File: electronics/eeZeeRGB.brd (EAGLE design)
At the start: 15.7 x 6.6 mm, 5 parts

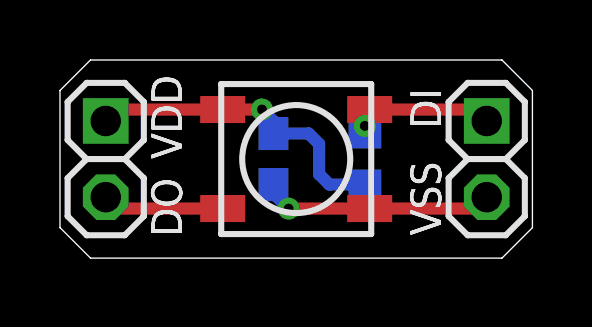
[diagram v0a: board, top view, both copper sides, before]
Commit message: added solder jumper to disable 10k pullup, moved passives layout, minor silk changes, changed silk for ws2812b
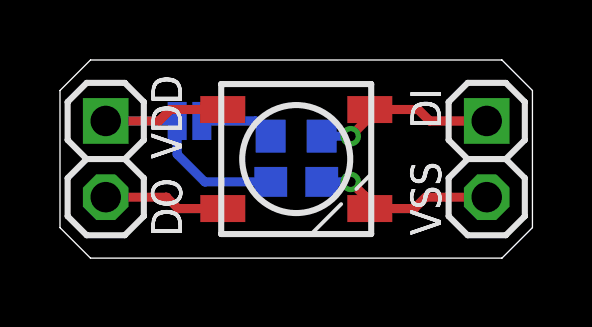
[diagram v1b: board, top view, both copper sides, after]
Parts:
- added SJ1: P/U?, SparkFun-Retired:SJ_2S
- moved R1 2.41 mm to (7.87, 4.06), turned to 0 degrees
- moved C1 1.08 mm to (7.87, 2.54), turned to 180 degrees
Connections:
- new net N$1: R1.2, SJ1.2
- net VDD: now also SJ1.1; no longer R1.2
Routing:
- net N$1: track 0.00 -> 2.50 mm
- net GND: track 7.77 -> 6.17 mm
- net DIN: track 4.88 -> 6.17 mm
- net VDD: track 10.7 -> 11.1 mm, vias 1 -> 0
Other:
- board text added: "R0.2"

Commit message: silk fixes for passives, shrunk board width, fixed version silk, moved pin labels after mirroring pin headers
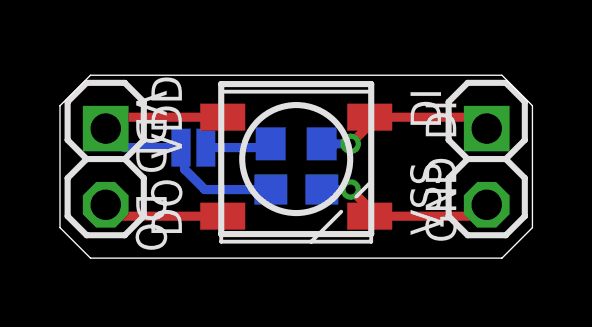
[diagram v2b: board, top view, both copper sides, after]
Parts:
- moved SJ1 0.90 mm to (4.45, 3.68)
- moved C1 0.25 mm to (7.87, 2.29)
- moved JP1 0.25 mm to (1.52, 3.05), flipped to the bottom
- moved JP2 0.25 mm to (14.2, 3.05), flipped to the bottom
- moved LED1 0.25 mm to (7.87, 3.05)
- moved R1 0.25 mm to (7.87, 3.81)
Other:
- board size 15.7 x 6.6 mm -> 15.7 x 6.1 mm
- board text added: "GND"
- board text added: "goo.gl/1GzN6m"

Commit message: Increased width to accommodate minimum width rule from OSHpark
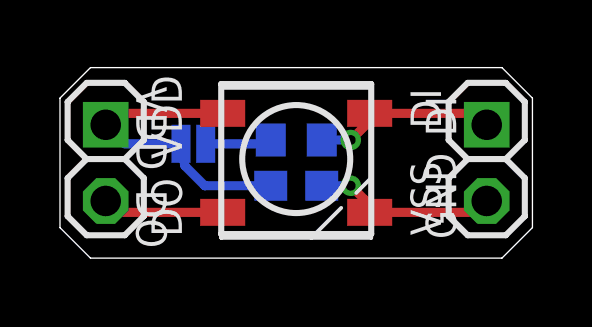
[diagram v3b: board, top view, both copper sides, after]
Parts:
- moved SJ1 0.13 mm to (4.45, 3.81)
- moved C1 0.13 mm to (7.87, 2.41)
- moved JP1 0.13 mm to (1.52, 3.17)
- moved JP2 0.13 mm to (14.2, 3.17)
- moved LED1 0.13 mm to (7.87, 3.17)
- moved R1 0.13 mm to (7.87, 3.94)
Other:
- board size 15.7 x 6.1 mm -> 15.7 x 6.3 mm
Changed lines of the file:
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@@
 <board>
 <plain>
-<wire x1="0" y1="5.08" x2="0" y2="1.016" width="0" layer="20"/>
+<wire x1="0" y1="5.334" x2="0" y2="1.016" width="0" layer="20"/>
 <wire x1="0" y1="1.016" x2="1.016" y2="0" width="0" layer="20"/>
 <wire x1="1.016" y1="0" x2="14.732" y2="0" width="0" layer="20"/>
 <wire x1="14.732" y1="0" x2="15.748" y2="1.016" width="0" layer="20"/>
-<wire x1="15.748" y1="1.016" x2="15.748" y2="5.08" width="0" layer="20"/>
-<wire x1="15.748" y1="5.08" x2="14.732" y2="6.096" width="0" layer="20"/>
-<wire x1="14.732" y1="6.096" x2="1.016" y2="6.096" width="0" layer="20"/>
-<wire x1="1.016" y1="6.096" x2="0" y2="5.08" width="0" layer="20"/>
-<text x="2.54" y="2.159" size="1.016" layer="21" font="vector" rot="SR270">DO</text>
-<text x="13.208" y="3.937" size="1.016" layer="21" font="vector" rot="R90">DI</text>
-<text x="13.208" y="0.508" size="1.016" layer="21" font="vector" rot="R90">GND</text>
-<text x="2.54" y="5.588" size="1.016" layer="21" font="vector" rot="SR270">VDD</text>
-<text x="11.938" y="4.826" size="1.016" layer="26" font="vector" rot="MR0">eeZeeRGB</text>
-<text x="7.747" y="0.508" size="0.8128" layer="26" font="vector" rot="MR0" align="bottom-center">goo.gl/1GzN6m</text>
+<wire x1="15.748" y1="1.016" x2="15.748" y2="5.334" width="0" layer="20"/>
+<wire x1="15.748" y1="5.334" x2="14.732" y2="6.35" width="0" layer="20"/>
+<wire x1="14.732" y1="6.35" x2="1.016" y2="6.35" width="0" layer="20"/>
+<wire x1="1.016" y1="6.35" x2="0" y2="5.334" width="0" layer="20"/>
+<text x="2.54" y="2.286" size="1.016" layer="21" font="vector" rot="SR270">DO</text>
+<text x="13.208" y="4.064" size="1.016" layer="21" font="vector" rot="R90">DI</text>
+<text x="13.208" y="0.635" size="1.016" layer="21" font="vector" rot="R90">GND</text>
+<text x="2.54" y="5.715" size="1.016" layer="21" font="vector" rot="SR270">VDD</text>
+<text x="11.938" y="4.953" size="1.016" layer="26" font="vector" rot="MR0">eeZeeRGB</text>
+<text x="7.747" y="0.635" size="0.8128" layer="26" font="vector" rot="MR0" align="bottom-center">goo.gl/1GzN6m</text>
 <text x="3.048" y="2.667" size="1.016" layer="121" font="vector" ratio="20" rot="R270">DO</text>
 <text x="12.7" y="4.318" size="1.016" layer="121" font="vector" ratio="20" rot="R90">DI</text>
@@
 <text x="5.715" y="4.699" size="1.016" layer="122" font="vector" ratio="20" rot="MR270">104</text>
 <text x="11.557" y="1.905" size="1.016" layer="122" font="vector" ratio="20" rot="MR90">10K</text>
-<text x="12.827" y="4.445" size="0.8128" layer="26" font="vector" rot="MR270">R0.2</text>
+<text x="12.827" y="4.572" size="0.8128" layer="26" font="vector" rot="MR270">R0.2</text>
 </plain>
 <attributes>
@@
 </autorouter>
 <elements>
-<element name="R1" library="rcl" package="R0603" value="10K" x="7.874" y="3.81" smashed="yes" rot="MR0">
-<attribute name="VALUE" x="9.398" y="4.318" size="0.8128" layer="28" font="vector" rot="MR180"/>
-</element>
-<element name="C1" library="rcl" package="C0603" value="104" x="7.874" y="2.286" smashed="yes" rot="MR180">
-<attribute name="VALUE" x="9.398" y="2.794" size="0.8128" layer="28" font="vector" rot="MR180"/>
-</element>
-<element name="LED1" library="bt_opto" package="WS2812B" value="WS2812B" x="7.874" y="3.048" smashed="yes"/>
-<element name="JP1" library="pinhead-2" package="1X02-S" value="" x="1.524" y="3.048" smashed="yes" rot="MR270">
-<attribute name="VALUE" x="4.699" y="5.588" size="1.27" layer="28" rot="MR270"/>
-</element>
-<element name="JP2" library="pinhead-2" package="1X02-S" value="" x="14.224" y="3.048" smashed="yes" rot="MR270">
-<attribute name="VALUE" x="17.399" y="5.588" size="1.27" layer="28" rot="MR270"/>
-</element>
-<element name="SJ1" library="SparkFun-Retired" package="SJ_2S" value="P/U?" x="4.445" y="3.683" smashed="yes" rot="MR180">
-<attribute name="VALUE" x="5.7758" y="1.651" size="0.8128" layer="28" font="vector" rot="MR0"/>
+<element name="R1" library="rcl" package="R0603" value="10K" x="7.874" y="3.937" smashed="yes" rot="MR0">
+<attribute name="VALUE" x="9.398" y="4.445" size="0.8128" layer="28" font="vector" rot="MR180"/>
+</element>
+<element name="C1" library="rcl" package="C0603" value="104" x="7.874" y="2.413" smashed="yes" rot="MR180">
+<attribute name="VALUE" x="9.398" y="2.921" size="0.8128" layer="28" font="vector" rot="MR180"/>
+</element>
+<element name="LED1" library="bt_opto" package="WS2812B" value="WS2812B" x="7.874" y="3.175" smashed="yes"/>
+<element name="JP1" library="pinhead-2" package="1X02-S" value="" x="1.524" y="3.175" smashed="yes" rot="MR270">
+<attribute name="VALUE" x="4.699" y="5.715" size="1.27" layer="28" rot="MR270"/>
+</element>
+<element name="JP2" library="pinhead-2" package="1X02-S" value="" x="14.224" y="3.175" smashed="yes" rot="MR270">
+<attribute name="VALUE" x="17.399" y="5.715" size="1.27" layer="28" rot="MR270"/>
+</element>
+<element name="SJ1" library="SparkFun-Retired" package="SJ_2S" value="P/U?" x="4.445" y="3.81" smashed="yes" rot="MR180">
+<attribute name="VALUE" x="5.7758" y="1.778" size="0.8128" layer="28" font="vector" rot="MR0"/>
 </element>
 </elements>
@@
 <contactref element="LED1" pad="DOUT"/>
 <contactref element="JP1" pad="2"/>
-<wire x1="5.424" y1="1.398" x2="1.904" y2="1.398" width="0.3048" layer="1"/>
-<wire x1="1.904" y1="1.398" x2="1.524" y2="1.778" width="0.3048" layer="1"/>
+<wire x1="5.424" y1="1.525" x2="1.904" y2="1.525" width="0.3048" layer="1"/>
+<wire x1="1.904" y1="1.525" x2="1.524" y2="1.905" width="0.3048" layer="1"/>
 </signal>
 <signal name="DIN">
@@
 <contactref element="LED1" pad="DIN"/>
 <contactref element="R1" pad="1"/>
-<wire x1="8.724" y1="3.81" x2="9.69" y2="3.81" width="0.3048" layer="16"/>
-<via x="9.69" y="3.81" extent="1-16" drill="0.3302"/>
-<wire x1="10.324" y1="4.698" x2="10.324" y2="4.444" width="0.3048" layer="1"/>
-<wire x1="10.324" y1="4.444" x2="9.69" y2="3.81" width="0.3048" layer="1"/>
-<wire x1="10.324" y1="4.698" x2="13.844" y2="4.698" width="0.3048" layer="1"/>
-<wire x1="13.844" y1="4.698" x2="14.224" y2="4.318" width="0.3048" layer="1"/>
+<wire x1="8.724" y1="3.937" x2="9.69" y2="3.937" width="0.3048" layer="16"/>
+<via x="9.69" y="3.937" extent="1-16" drill="0.3302"/>
+<wire x1="10.324" y1="4.825" x2="10.324" y2="4.571" width="0.3048" layer="1"/>
+<wire x1="10.324" y1="4.571" x2="9.69" y2="3.937" width="0.3048" layer="1"/>
+<wire x1="10.324" y1="4.825" x2="13.844" y2="4.825" width="0.3048" layer="1"/>
+<wire x1="13.844" y1="4.825" x2="14.224" y2="4.445" width="0.3048" layer="1"/>
 </signal>
 <signal name="GND">
@@
 <contactref element="LED1" pad="VSS"/>
 <contactref element="JP2" pad="2"/>
-<wire x1="8.724" y1="2.286" x2="9.69" y2="2.286" width="0.3048" layer="16"/>
-<via x="9.69" y="2.286" extent="1-16" drill="0.3302"/>
-<wire x1="10.324" y1="1.398" x2="10.324" y2="1.614" width="0.3048" layer="1"/>
-<wire x1="10.324" y1="1.614" x2="10.16" y2="1.778" width="0.3048" layer="1"/>
-<wire x1="10.16" y1="1.778" x2="10.16" y2="1.816" width="0.3048" layer="1"/>
-<wire x1="10.16" y1="1.816" x2="9.69" y2="2.286" width="0.3048" layer="1"/>
-<wire x1="10.324" y1="1.398" x2="13.844" y2="1.398" width="0.3048" layer="1"/>
-<wire x1="13.844" y1="1.398" x2="14.224" y2="1.778" width="0.3048" layer="1"/>
+<wire x1="8.724" y1="2.413" x2="9.69" y2="2.413" width="0.3048" layer="16"/>
+<via x="9.69" y="2.413" extent="1-16" drill="0.3302"/>
+<wire x1="10.324" y1="1.525" x2="10.324" y2="1.741" width="0.3048" layer="1"/>
+<wire x1="10.324" y1="1.741" x2="10.16" y2="1.905" width="0.3048" layer="1"/>
+<wire x1="10.16" y1="1.905" x2="10.16" y2="1.943" width="0.3048" layer="1"/>
+<wire x1="10.16" y1="1.943" x2="9.69" y2="2.413" width="0.3048" layer="1"/>
+<wire x1="10.324" y1="1.525" x2="13.844" y2="1.525" width="0.3048" layer="1"/>
+<wire x1="13.844" y1="1.525" x2="14.224" y2="1.905" width="0.3048" layer="1"/>
 </signal>
 <signal name="VDD">
@@
 <contactref element="JP1" pad="1"/>
 <contactref element="SJ1" pad="1"/>
-<wire x1="7.024" y1="2.286" x2="4.826" y2="2.286" width="0.3048" layer="16"/>
-<wire x1="4.826" y1="2.286" x2="4.1601" y2="2.9519" width="0.3048" layer="16"/>
-<wire x1="4.0331" y1="3.683" x2="4.1601" y2="2.9519" width="0.3048" layer="16"/>
-<wire x1="5.424" y1="4.698" x2="1.904" y2="4.698" width="0.3048" layer="1"/>
-<wire x1="1.904" y1="4.698" x2="1.524" y2="4.318" width="0.3048" layer="1"/>
-<wire x1="4.0331" y1="3.683" x2="2.159" y2="3.683" width="0.3048" layer="16"/>
-<wire x1="2.159" y1="3.683" x2="1.524" y2="4.318" width="0.3048" layer="16"/>
+<wire x1="7.024" y1="2.413" x2="4.826" y2="2.413" width="0.3048" layer="16"/>
+<wire x1="4.826" y1="2.413" x2="4.1601" y2="3.0789" width="0.3048" layer="16"/>
+<wire x1="4.0331" y1="3.81" x2="4.1601" y2="3.0789" width="0.3048" layer="16"/>
+<wire x1="5.424" y1="4.825" x2="1.904" y2="4.825" width="0.3048" layer="1"/>
+<wire x1="1.904" y1="4.825" x2="1.524" y2="4.445" width="0.3048" layer="1"/>
+<wire x1="4.0331" y1="3.81" x2="2.159" y2="3.81" width="0.3048" layer="16"/>
+<wire x1="2.159" y1="3.81" x2="1.524" y2="4.445" width="0.3048" layer="16"/>
 </signal>
 <signal name="N$1">
 <contactref element="SJ1" pad="2"/>
 <contactref element="R1" pad="2"/>
-<wire x1="4.8569" y1="3.683" x2="6.858" y2="3.683" width="0.3048" layer="16"/>
-<wire x1="6.858" y1="3.683" x2="7.024" y2="3.81" width="0.3048" layer="16"/>
+<wire x1="4.8569" y1="3.81" x2="6.858" y2="3.81" width="0.3048" layer="16"/>
+<wire x1="6.858" y1="3.81" x2="7.024" y2="3.937" width="0.3048" layer="16"/>
 </signal>
 </signals>
